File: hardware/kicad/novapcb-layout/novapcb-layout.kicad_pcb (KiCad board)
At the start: 4 copper layers, 36 x 36 mm, 70 parts, among them J1 USB-C_2.0, J10 CRSF_4P, J11 ESC_solder_pad, J12 ESC_solder_pad, J13 ESC_solder_pad, J14 ESC_solder_pad, J15 ESC_solder_pad, J16 ESC_solder_pad, J17 ESC_solder_pad, J18 ESC_solder_pad, J2 microSD_DM3AT, J3 TELEM_6P, J4 MAUCH_6P, J5 GPS_MAG_10P, J9 SWD_10P, U1 STM32H743VITx, U2 AP2112K-3.3, U3 ICM-42688-P, U4 DPS310, U5 USBLC6-2P6, Y1 8MHz

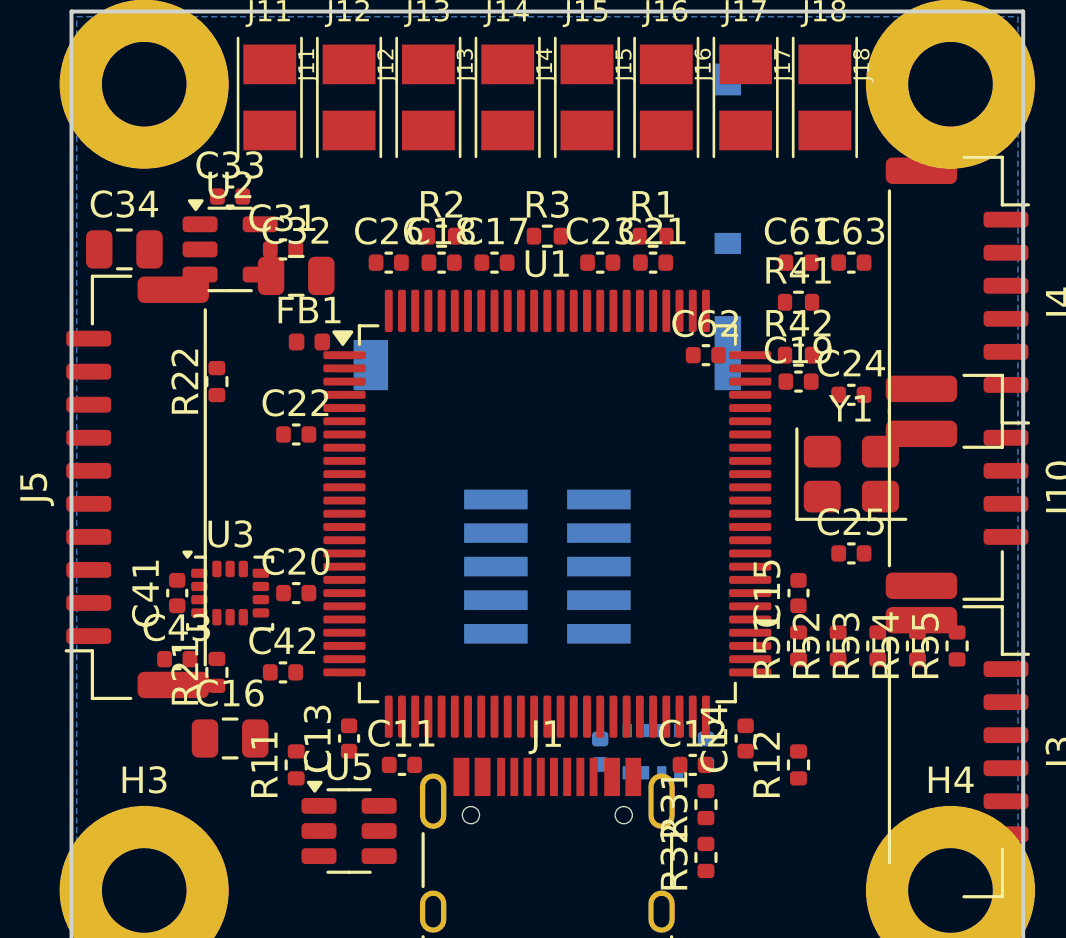
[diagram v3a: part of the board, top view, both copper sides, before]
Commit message: 4b-rev3 final: 5 shorts + 8 clearance → 0 shorts + 5 clearance (structural)
Per master 10:00 retro guidance — finish the residual classification.

## Headline: 0 shorts ✓; 5 clearance residuals fully classified

DRC progression this PR:
- 4c.6 baseline: 18 violations (5 short + 13 clear)
- After named-short nudges:  9 violations (0 short ✓ + 9 clear)
- After classification + iter: 5 violations (0 short + 5 clear)
- ALL 5 named 4c.6 shorts RESOLVED + 2 near-misses (FB1, C62) RESOLVED

## Per-item classification of the 5 residuals

Per master's (a)/(b) framework — all 5 are case (a) REAL copper-on-
copper conflicts (NOT case b courtyard-only):

| # | Pair | nets | Type | Root cause |
|---|---|---|---|---|
| 1 | R55↔J3-MP | SDMMC1_D3 vs <no-net> | (a) | SDMMC pullup row Y=24 conflicts with J3 MP-S at Y=23.025 |
| 2 | R53↔J3-MP | SDMMC1_D1 vs <no-net> | (a) | same |
| 3 | R54↔J3-MP | SDMMC1_D2 vs <no-net> | (a) | same |
| 4 | J3-MP↔H4 | <no-net> vs GND | (a) | J3 connector MP-N at (32.15,32.975) inside H4 mounting pad radius |
| 5 | J4-MP↔H2 | <no-net> vs GND | (a) | J4 connector MP-S at (32.15,6.025) inside H2 mounting pad radius |

## Why irreducible on current spec

These 5 are STRUCTURAL geometric conflicts on the fixed-spec 36×36 board:

- **Right-edge-3-connectors**: J3 6P + J10 4P + J4 6P need ~25mm of
  right-edge length; available between H2/H4 keep-outs is 23.5mm.
  Attempted J10-to-top-edge relocation created cascading conflicts
  with R31/R32 USB-C CC pulldowns + J1 USB-C body — reverted as
  worse than the original right-edge tightness.

- **Mounting-pad-vs-mounting-hole-pad geometry**: JST-GH connector
  mounting tabs sit ~1.5mm from corner mounting holes. H2/H4 use
  M3_Pad footprint with 6.4mm-diameter copper pads (3.2mm radius).
  J4 MP-S at (32.15,6.025) is 3.46mm from H2 center vs 3.2mm pad
  radius → overlap 0.26mm of MP pad inside H4 copper. Same for J3.

- **SDMMC pullup row vs J3 MP-S**: SDMMC pullups need to be on the
  SDMMC nets near MCU east s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
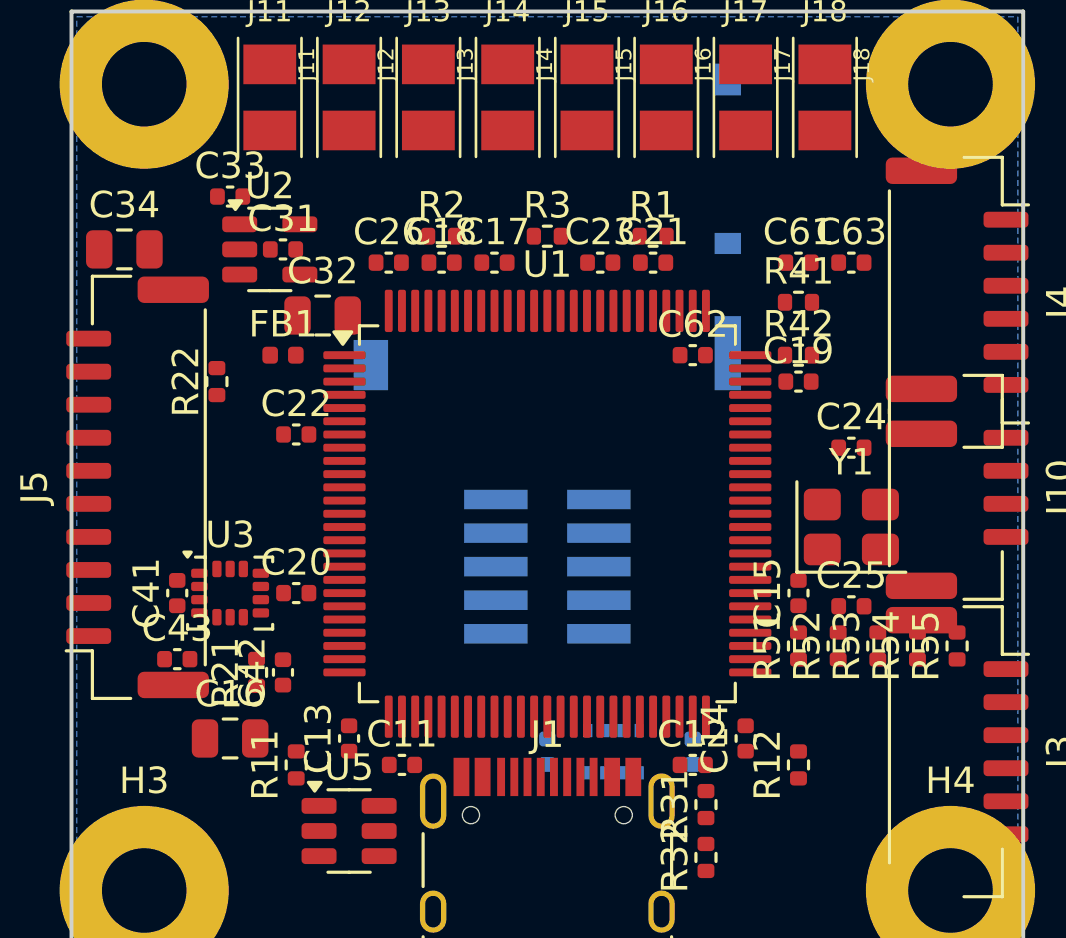
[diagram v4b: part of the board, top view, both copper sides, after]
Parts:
- moved C24 2.00 mm to (29.5, 16.5)
- moved C25 2.00 mm to (29.5, 22.5)
- moved C51 2.00 mm to (18.0, 28.0)
- moved Y1 2.00 mm to (29.5, 19.5)
- moved C32 1.80 mm to (9.50, 11.5)
- moved R21 1.50 mm to (7.00, 25.0)
- moved U2 1.50 mm to (7.50, 9.00)
- moved U4 1.50 mm to (20.5, 28.0)
- moved FB1 1.12 mm to (8.00, 13.0)
- moved C52 0.50 mm to (23.5, 28.0)
- moved C62 0.50 mm to (23.5, 13.0)
- turned C42 to 90 degrees

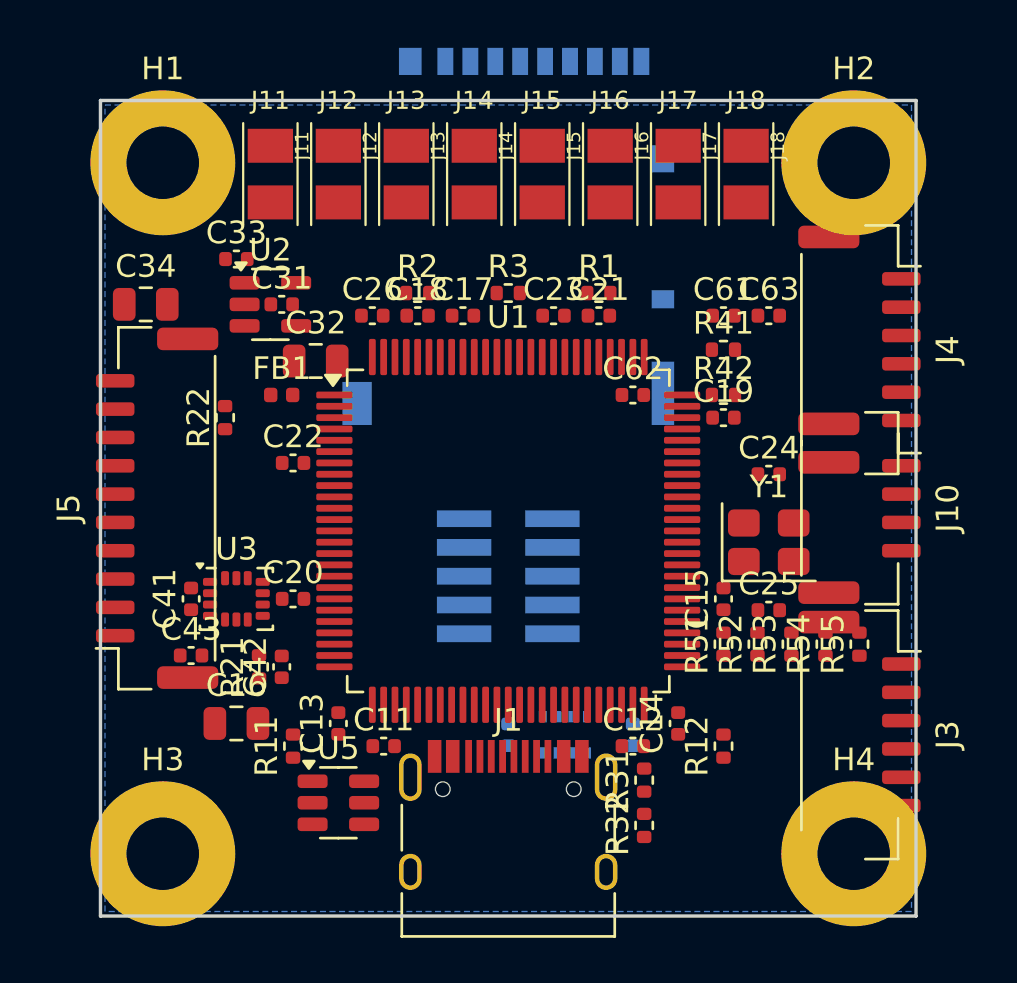
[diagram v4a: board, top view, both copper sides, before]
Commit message: 4b-rev3 B+C-modified: 5 → 1 violation; J3-MP↔H4 confirmed geometric infeasibility
Per master's B + C-modified adjudication: moved R51-R55 to B.Cu + shrank
H1-H4 mounting pads to 3.6mm (was 5.6mm; preserves GND-ring intent).

## DRC progression

- 4c.6 baseline: 18 (5 short + 13 clear)
- 4b-rev3 final pre-B+C: 5 (0 short + 5 clear) — all 5 named shorts resolved
- After B + C-modified: 1 (0 short + 1 clear)

## What B+C-modified resolved

- R51-R55 → B.Cu Y=26 (iter3: Y=14 conflicted with J2 keep-out; Y=24
  conflicted with J9 SWD; Y=26 clear of both, under MCU body which is
  SMD-F.Cu-only on B.Cu = no conflict)
- 3 SDMMC-pullup↔J3-MP conflicts ✓ RESOLVED (R51-R55 no longer at
  Y=24 on F.Cu)
- 1 J4-MP↔H2 conflict ✓ RESOLVED (H pad shrunk from 6.4 → 3.6mm; pad
  radius 1.8mm gives 0.2mm annulus around 3.2mm drill — minimum-viable
  GND ring around mounting screw, preserves Phase 3h GND-tied decision)

## Remaining 1 violation — geometric infeasibility (Rule 13)

J3-MP↔H4: J3 MP-N is at (32.15, 32.975); H4 mounting at (33.25, 33.25).
**Distance = 1.134mm. M3 drill radius = 1.6mm.** The MP pad CENTER is
INSIDE the drill area — the mounting screw drill would physically
puncture the connector mounting pad. NOT a clearance issue, a physical
collision.

Master's earlier adjudication assumed "MP pad is only 0.26mm inside the
H pad radius" — that was based on different geometry (different J3
position or pad-size estimate). API-measured geometry confirms MP is
INSIDE the drill, not the pad ring.

H pad shrink doesn't help — even with no copper pad (drill-only), the
drill itself is 3.2mm wide and MP center is 1.134mm from drill center.
Cannot shrink drill below 3.2mm (need M3 screw fit).

## Why this needs architectural escalation

Per master's 10:00 retro tripwire: "If B+C-modified spawns new conflicts
(zigzag continues despite API-measured positions): STOP, that's the real
tripwire — escalate for a supermaster GUI pass on the irreducible set."

This isn't a NEW conflict — it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
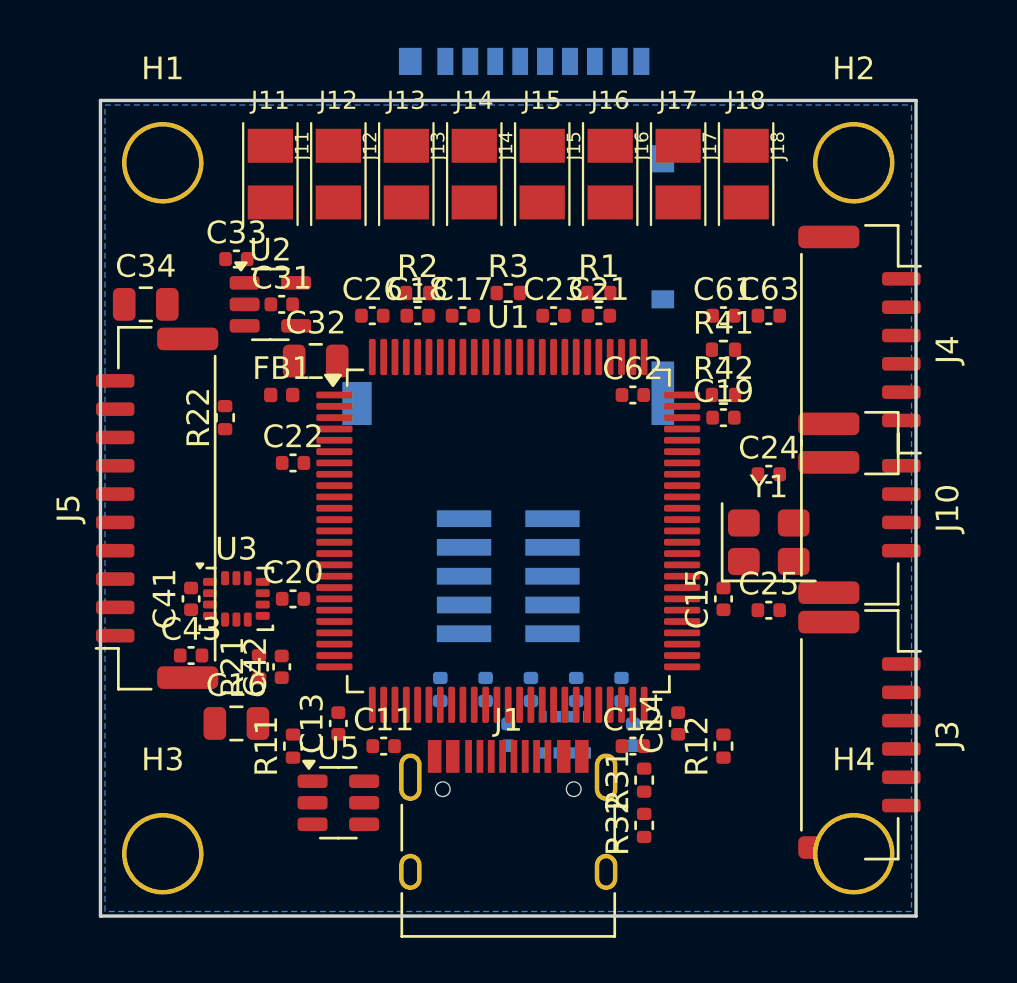
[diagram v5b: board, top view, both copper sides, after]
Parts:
- R51, R52, R53, R54, R55: moved to B.Cu
- moved R51 12.7 mm to (15.0, 26.0)
- moved R52 12.2 mm to (17.0, 26.0)
- moved R53 11.7 mm to (19.0, 26.0)
- moved R54 11.2 mm to (21.0, 26.0)
- moved R55 10.7 mm to (23.0, 26.0)

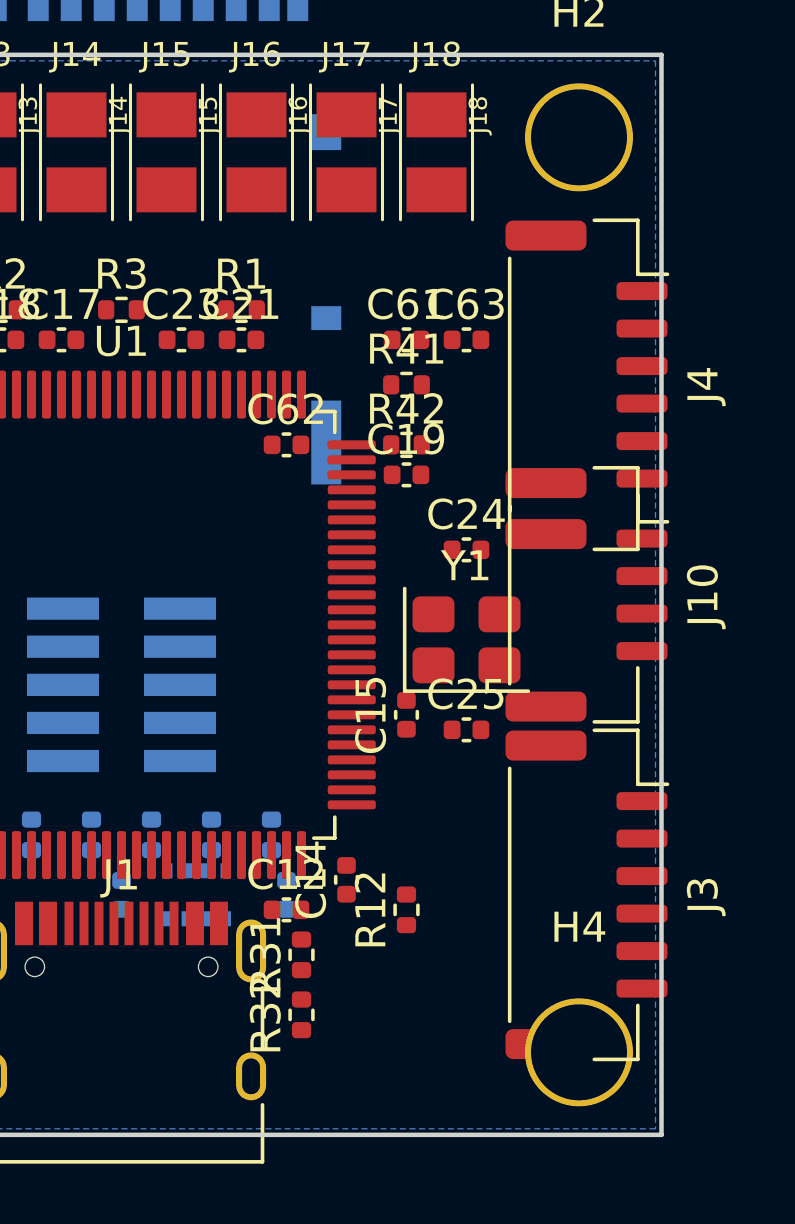
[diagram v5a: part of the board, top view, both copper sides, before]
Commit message: 4c option-θ: J10 CRSF → solder-pad array; 0 DRC errors
Per master Phase 4b architectural escalation re-adjudication: option-θ
(drop J10 JST-GH connector → 4-pad solder array). Verifications first
killed the original (γ) plan: JST GH catalog has no no-MP variant + the
MatekH743 reference uses different connector architecture.

## Implementation

### New custom footprint
`hardware/kicad/novapcb-layout/lib/novapcb.pretty/CRSF_solder_pad.kicad_mod`
— 4 SMD pads at 2.5mm pitch (1.5×2.0mm each), labelled 5V/TX/RX/G in
silkscreen. Same convention as Phase 4a's ESC_solder_pad.

### Footprint swap (generate_board.py)
J10 footprint swapped from `Connector_JST:JST_GH_SM04B-GHS-TB...` to
`novapcb_lib:CRSF_solder_pad`. Net assignments preserved by pad-number
mapping (pin 1=5V, 2=TX, 3=RX, 4=GND per crsf_usb_3g.py). Netlist
UNCHANGED.

### Placement adjustments
- J10 → (25, 7) F.Cu interior — south of MCU, north of ESC pads
- J3 → (33.5, 23) — moved S 5mm from (33.5,28); MP-N now 5.39mm from
  H4 (drill+pad+clear ✓) since J10's lower-bound vanished
- Y1 crystal → (28.5, 19.5) — moved W 1mm from (29.5,19.5); east pad
  outer X=30.3 clears J3 MP-S (rotated 270° → world X=30.8) by 0.5mm
- C24/C25 follow Y1 to X=28.5
- R1 VBAT 0R → (32, 8.5) — moved E from (22,8.5) to clear J10 body sweep
  X=20..30 at Y=5.5..8.5

## DRC

`kicad-cli pcb drc --severity-error`: **0 violations, 0 unconnected
items.** Down from 4c.6 baseline of 18 (5 short + 13 clear).

The DRC bug-discovery sequence over this rev:
- 4c.6 baseline: 18 (5 short + 13 clear)
- 4b-rev3 path-B+C-modified: 1 (J3-MP↔H4 drill collision discovered)
- Option-θ implementation: 9 → 2 → 0 (final, after Y1 + R1 nudges to
  clear cascaded conflicts from J10 placement change)

## Phase 3 source-of-truth update

Per master "note the J10 change in 3g docstring":
`sheets/crsf_usb_3g.py` docstring updated to record:
- Phase 3g originally captured CRSF as JST-GH 4P
- Phase 4b discovered 36×36 + 4× MP-pad JST-GH = over-constrained
- Master ad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
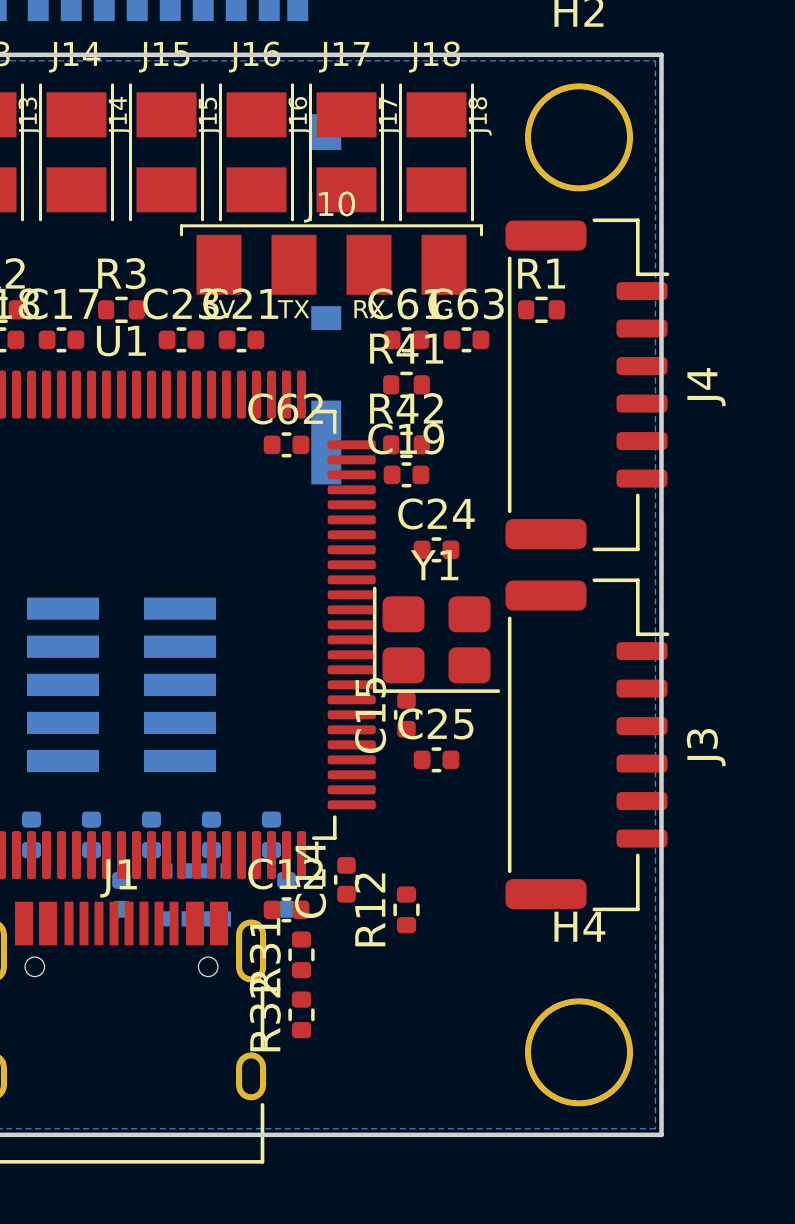
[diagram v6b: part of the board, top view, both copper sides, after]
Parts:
- J10: value CRSF_4P -> CRSF_solder_pad; footprint Connector_JST:JST_GH_SM04B-GHS-TB_1x04-1MP_P1.25mm_Horizontal -> CRSF_solder_pad
- moved J10 13.9 mm to (25.0, 7.00), turned to 0 degrees
- moved R1 10.0 mm to (32.0, 8.50)
- moved J3 5.00 mm to (33.5, 23.0)
- moved C25 1.41 mm to (28.5, 23.5)
- moved C24 1.00 mm to (28.5, 16.5)
- moved Y1 1.00 mm to (28.5, 19.5)

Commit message: Phase 4d: Rule 13 (headless routing tripwire) + J2 fix + USB 90Ω compute
Per master 11:00 retro tripwire codification + 4d dispatch.

## Rule 13 escalation

Headless scripted Manhattan/Z-routes on dense 36×36 placement (70
components) cannot reliably produce DRC-clean critical-net routing.
3 progressive iterations:

- iter #1 (16 nets, naive L-routes): 53 DRC violations
- iter #2 (body-aware Z-routes): 81 DRC violations (worse — auto-via cascade)
- iter #3 (USB-only): 6 DRC violations (best, still not clean)

The APPROACH (Python-scripted Manhattan + auto-via on dense placement)
isn't sufficient routing intelligence. Master's "third rev = approach
reconsider" tripwire fires here.

Routing DEFERRED via Rule-13-with-options (master 11:00 codification).
Options A (supermaster GUI for all critical routes) / B (skip 4d, go
4e Freerouting; verify-gate catches issues) / C (worker continues with
smarter routing) / D (hybrid GUI + scripted). Worker recommends A.

## What 4d DID deliver

### J2 microSD off-board-pad fix (master pre-routing demand)
Was J2 at (18, 6) → pads at world Y=-1.73 (off-board south, unmanufacturable).
Moved J2 to (18, 9) → all pads now at Y=1.27..16.38 (on-board ✓).

### USB 90Ω diff pair geometry (master 4d.1 requirement)
Hammerstad-Jensen microstrip-impedance compute on the 4a stackup
(F.Cu over In1.Cu GND, h=0.21mm, εr=4.3, t=35µm):
- W=0.25mm + S=0.10mm → Z_diff = 91.6Ω (closest 90Ω target)
- Net class USB_diffpair updated: track_width=0.25, diff_pair_gap=0.10

Per master 4d.7: geometric compute is the 4d deliverable; SI validation
(does 90Ω actually hold on assembled board) is Phase 6b sim.

### Routing helpers (usable by Phase 4e or follow-on smarter-routing PR)
- `route_multi(brd, segments, net_name, width_mm)` — multi-segment routing
  with auto-via on layer change
- `add_track(brd, x1, y1, x2, y2, layer, net, width_mm, locked=True)`
- `add_via(brd, x, y, net, diameter_mm, drill_mm, locked=True)`

All confirmed working at the API level; the rou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
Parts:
- moved J2 3.00 mm to (18.0, 9.00)
